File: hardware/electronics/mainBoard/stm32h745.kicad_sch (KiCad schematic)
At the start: 54 parts, among them SW1 PTS810, SW2 PTS810, U1 STM32H745ZIT6

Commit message: debugger stuff
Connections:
- net EEPROM_WC: now also U1.28 (PC0); no longer U1.127 (PG14)
- net H7_LEDBUILTIN: now also U1.40 (PA3); no longer U1.37 (PA0)
- net LTE.PWR_EN: now also U1.9 (PC13); no longer U1.5 (PE6)
- net LTE.RST: now also U1.5 (PE6); no longer U1.1 (PE2)
- net QSPI1.IO2: now also U1.1 (PE2); no longer U1.21 (PF7)
- net SDMMC2.CMD: now also U1.37 (PA0); no longer U1.121 (PD7)
- net USART6.TX: now also U1.127 (PG14); no longer U1.93 (PC6)
- net UART7.RX: now reaches U1.57 (PE7)
- net L0_NRST renamed L0_nRST
- new net UART7.TX: U1.21 (PF7)
- no-connect marks 31 -> 29
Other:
- note added: "Check CANBus RX/RX In/Out"
- moved on the sheet: D1, R1

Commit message: nets
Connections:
- net H7_NRST: no longer C1.1, D2.1, SW1.1, SW1.2, U1.27 (NRST)
- net 25MHz renamed H7_25MHz
- net 32768Hz renamed H7_32768Hz
- new net H7_nRST: C1.1, D2.1, SW1.1, SW1.2, U1.27 (NRST)
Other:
- note removed: "Check CANBus RX/RX In/Out"
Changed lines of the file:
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@@
 		)
 	)
-	(text "Check CANBus RX/RX In/Out"
-		(exclude_from_sim no)
-		(at 92.71 60.96 0)
-		(effects
-			(font
-				(size 1.27 1.27)
-			)
-		)
-	)
 	(text "AUX Card GPIO"
 		(exclude_from_sim no)
@@
 		)
 	)
-	(label "25MHz"
+	(label "H7_25MHz"
 		(at 171.45 45.72 180)
 		(effects
@@
 		)
 	)
-	(label "H7_NRST"
+	(label "H7_nRST"
 		(at 168.91 71.12 180)
 		(effects
@@
 		)
 	)
-	(label "32768Hz"
+	(label "H7_32768Hz"
 		(at 93.98 55.88 180)
 		(effects
@@
 		)
 	)
-	(hierarchical_label "25MHz"
+	(hierarchical_label "H7_25MHz"
 		(shape input)
 		(at 171.45 45.72 0)
@@
 		)
 	)
-	(hierarchical_label "32768Hz"
+	(hierarchical_label "H7_32768Hz"
 		(shape input)
 		(at 93.98 55.88 0)
@@
 		)
 	)
-	(hierarchical_label "H7_NRST"
+	(hierarchical_label "H7_nRST"
 		(shape input)
 		(at 171.45 71.12 0)
@@
 			(justify left bottom)
 		)
-		(property "Netclass" "MII"
+		(property "Netclass" "RMII"
 			(at 240.7285 13.97 0)
 			(effects

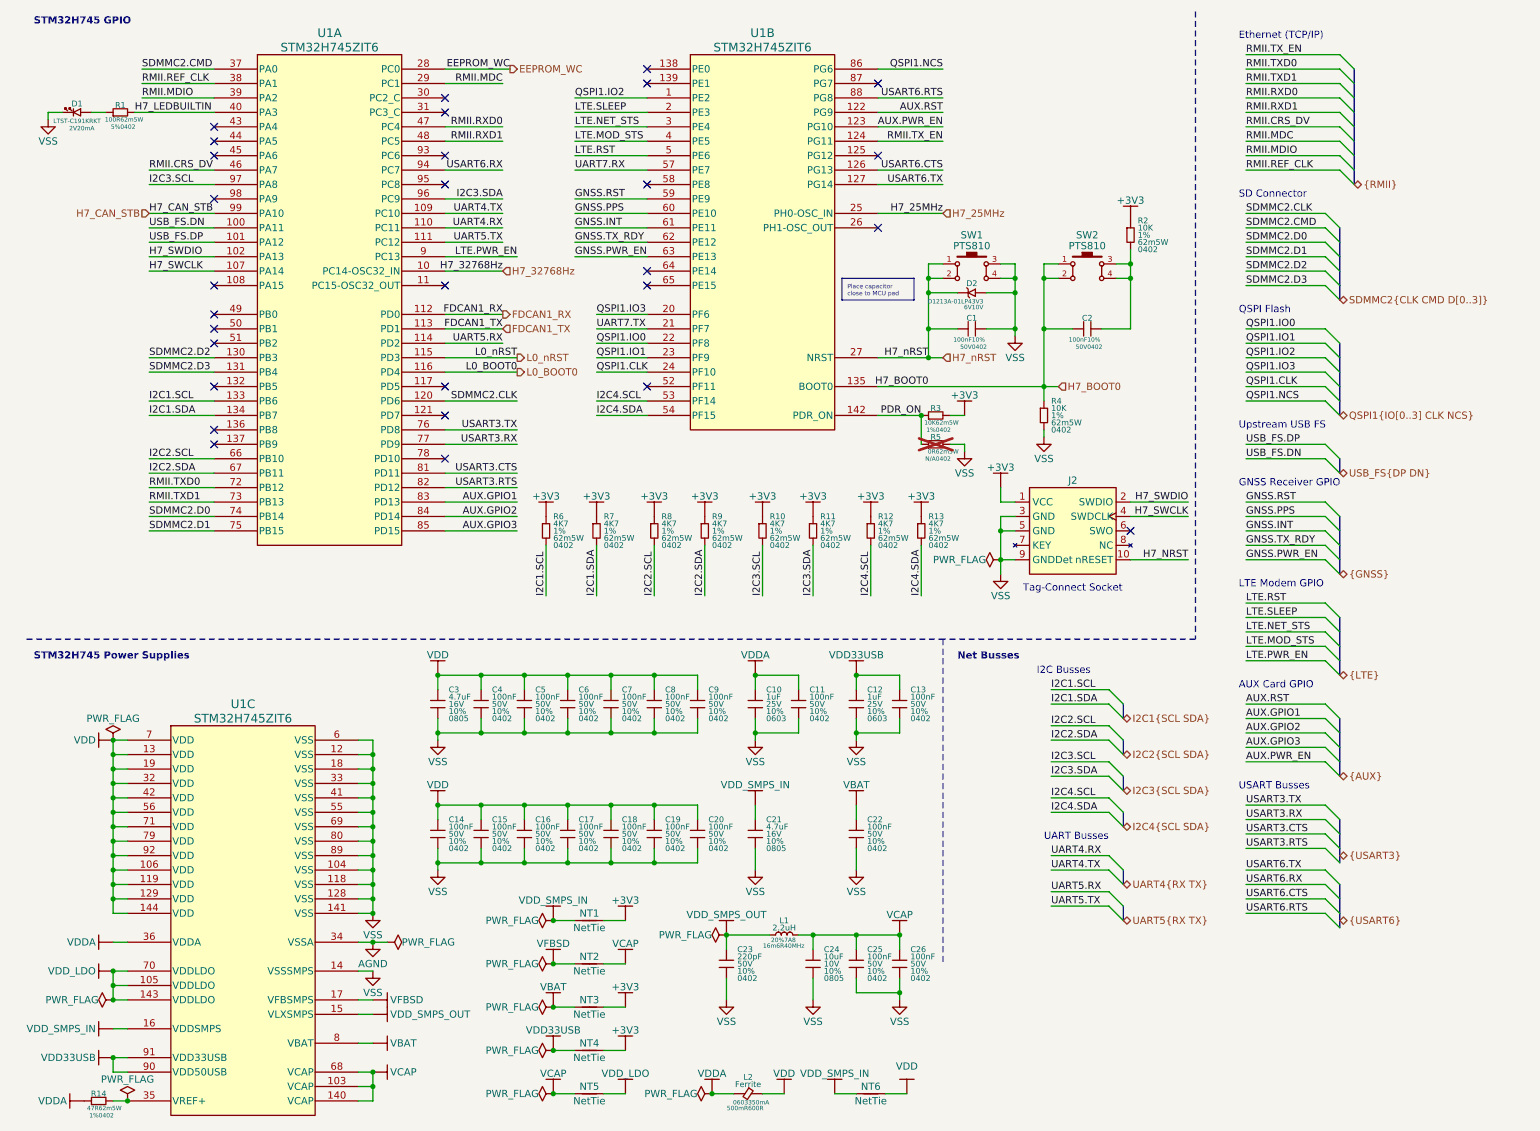
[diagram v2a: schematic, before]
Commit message: fixed net names
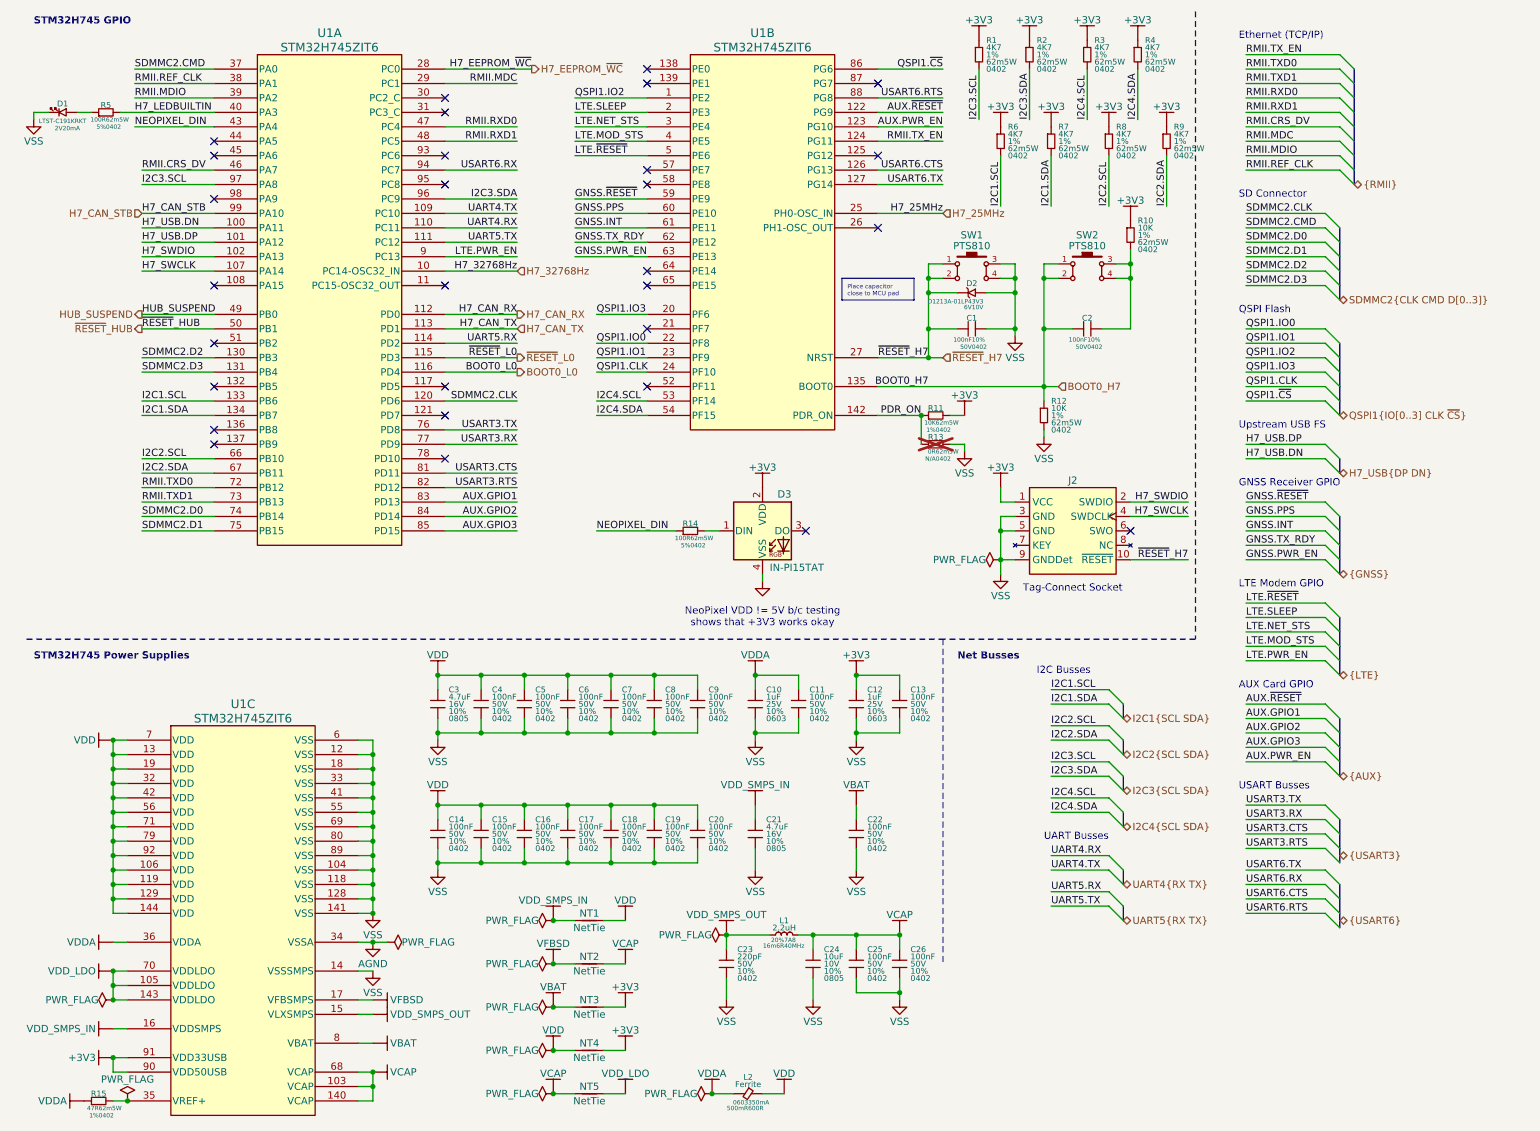
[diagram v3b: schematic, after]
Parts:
- removed NT6: NetTie, lib_misc:NetTie-2_SMD_Pad2.0mm, symbol lib_sch:NetTie
- added D3: IN-PI15TAT, lib_diodes:IN-PI15TAT, symbol lib_sch:Addressable LED
- added R14: 100R, lib_passives:CRCW0402, symbol lib_sch:R_horizontal
- renumbered R10 to R1, R2 to R10, R3 to R11, R4 to R12, R5 to R13, R14 to R15, R11 to R2, R12 to R3, R13 to R4, R1 to R5
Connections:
- net H7_nRST is gone; now on net ~{RESET}_H7: C1.1, D2.1, SW1.1, SW1.2, U1.27 (NRST)
- net +3V3: now also C12.1, C13.1, U1.90 (VDD50USB), U1.91 (VDD33USB), D3.2 (VDD); no longer NT1.2
- net VDD: now also NT1.2, NT4.1
- net VSS: now also D3.4 (VSS)
- net NEOPIXEL_DIN: now reaches U1.43 (PA4)
- net NEOPIXEL_DIN: now also R14.1
- net HUB_SUSPEND: now reaches U1.49 (PB0)
- net ~{RESET}_HUB: now reaches U1.50 (PB1)
- net AUX.RST renamed AUX.~{RESET}
- net EEPROM_WC renamed H7_EEPROM_~{WC}
- net FDCAN1_RX renamed H7_CAN_RX
- net FDCAN1_TX renamed H7_CAN_TX
- net GNSS.RST renamed GNSS.~{RESET}
- net H7_BOOT0 renamed BOOT0_H7
- net H7_NRST renamed ~{RESET}_H7
- net L0_BOOT0 renamed BOOT0_L0
- net L0_nRST renamed ~{RESET}_L0
- net LTE.RST renamed LTE.~{RESET}
- net QSPI1.NCS renamed QSPI1.~{CS}
- net UART7.RX: no longer names the net of U1.57 (PE7)
- net UART7.TX: no longer names the net of U1.21 (PF7)
- net USB_FS.DN renamed H7_USB.DN
- net USB_FS.DP renamed H7_USB.DP
- removed net VDD33USB: C12.1, C13.1, NT4.1, U1.90 (VDD50USB), U1.91 (VDD33USB)
- new net: D3.1 (DIN), R14.2
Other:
- note added: "NeoPixel VDD != 5V b/c testing shows that +3V3 works okay"
- moved on the sheet: D1, R1, R2, R3, R4, R5, R6, R7, R8, R9

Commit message: power supplies and organization
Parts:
- removed C1: 100nF, lib_passives:GCM0402, symbol lib_sch:C_horizontal
- removed C10, C12: 1uF, lib_passives:GRT0603, symbol lib_sch:C
- removed C11, C13, C22: 100nF, lib_passives:GCM0402, symbol lib_sch:C
- removed C21, C3: 4.7uF, lib_passives:GCM0805, symbol lib_sch:C
- removed NT1, NT2, NT3, NT4, NT5: NetTie, lib_misc:NetTie-2_SMD_Pad2.0mm, symbol lib_sch:NetTie
- added C148, C149, C152, C155, C159, C160: 100nF, lib_passives:GCM0402, symbol lib_sch:C
- added C150: 1uF, lib_passives:GRT0603, symbol lib_sch:C
- added C151, C154: 4.7uF, lib_passives:GCM0805, symbol lib_sch:C
- added C153, C158: 10uF, lib_passives:GCM0805, symbol lib_sch:C
- added C156, C157: 2.2uF, lib_passives:GCM0805, symbol lib_sch:C
- added C3: 100nF, lib_passives:GCM0402, symbol lib_sch:C_horizontal
- added JP9: Jumper_3_Bridged12, symbol lib_sch:Jumper_3_Bridged12
- U1: footprint lib_ICs:LQFP-144 -> LQFP-144
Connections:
- net AGND is gone; now on net VSS: U1.34 (VSSA)
- net VBAT is gone; now on net +3V3: U1.8 (VBAT)
- net VDD_SMPS_IN is gone; now on net +3V3: U1.16 (VDDSMPS)
- net +3V3: now also C14.1, C15.1, C16.1, C17.1, C18.1, C19.1, C20.1, C4.1, C5.1, C6.1, C7.1, C8.1, C9.1, L2.1, U1.106 (VDD), U1.119 (VDD), U1.129 (VDD), U1.13 (VDD), U1.144 (VDD), U1.19 (VDD), U1.32 (VDD), U1.42 (VDD), U1.56 (VDD), U1.7 (VDD), U1.71 (VDD), U1.79 (VDD), U1.92 (VDD), C148.1, C150.1, C151.1, C153.1, C154.1, C155.1, C160.1
- net I2C2.SCL: now also R9.2; no longer R8.2
- net I2C2.SDA: now also R8.2; no longer R9.2
- net VCAP: now also C156.1, C157.1, JP9.1 (A); no longer C24.1, L1.2
- net VDDA: now also L2.2, C158.1, C159.1; no longer L2.1
- net VDD_LDO: now also C149.1, C152.1, JP9.3 (B)
- net VSS: now also C148.2, C149.2, C150.2, C151.2, C152.2, C153.2, C154.2, C155.2, C156.2, C157.2, C158.2, C159.2, C160.2, C3.2
- net ~{RESET}_H7: now also C3.1
- removed net VDD: C14.1, C15.1, C16.1, C17.1, C18.1, C19.1, C20.1, C4.1, C5.1, C6.1, C7.1, C8.1, C9.1, L2.2, U1.106 (VDD), U1.119 (VDD), U1.129 (VDD), U1.13 (VDD), U1.144 (VDD), U1.19 (VDD), U1.32 (VDD), U1.42 (VDD), U1.56 (VDD), U1.7 (VDD), U1.71 (VDD), U1.79 (VDD), U1.92 (VDD)
- net VDD_SMPS_OUT: no longer names the net of C23.1, U1.15 (VLXSMPS)
- net VDD_SMPS_OUT: now also L1.2; no longer L1.1
- net VFBSD renamed SMPS_FB
- net SMPS_FB: now also C24.1, L1.1, JP9.2 (C)
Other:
- note added: "M.2 GPIO"
- note added: "VBAT"
- note added: "VDD"
- note added: "VDDA"
- note added: "VDDLDO"
- note added: "VDDSMPS"
- note added: "VDDUSB"
- note removed: "AUX Card GPIO"
- note removed: "GNSS Receiver GPIO"
- note removed: "LTE Modem GPIO"
- moved on the sheet: C14, C15, C16, C17, C18, C19, C2, C20, C23, C24, C25, C26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

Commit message: organized page. Added SPI and other nets
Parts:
- added Q1: BSS138-7-F, lib_ICs:SOT23, symbol lib_sch:NMOS_GSD
- JP1: renamed from JP9; footprint (none) -> lib_misc:SolderJumper-3_P1.3mm_Bridged12_RoundedPad1.0x1.5mm
- L1: renamed from L2; now not fitted
- R14: renamed from R5; value 100R -> 412R; DKPN 541-100JCT-ND -> 541-412LCT-ND; MPN CRCW0402100RJNED -> CRCW0402412RFKED
- U1: footprint LQFP-144 -> lib_ICs:LQFP-144
- renumbered C3 to C1, C14 to C10, C15 to C11, C16 to C12, C17 to C13, C18 to C14, C19 to C15, C20 to C16, C153 to C17, C158 to C18, C159 to C19, C154 to C20, C155 to C21, C150 to C22, C148 to C23, C149 to C24, C152 to C25, C160 to C26, C24 to C27, C23 to C28, C156 to C29, C151 to C3, C157 to C30, C26 to C31, C25 to C32, D2 to D1, D3 to D2, D1 to D3, L1 to L2, R11 to R10, R12 to R11, R13 to R12, R14 to R13, R10 to R3, R8 to R4, R9 to R5, R7 to R6, R6 to R7, R4 to R8, R3 to R9
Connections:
- net H7_LEDBUILTIN: now also R14.1, U1.136 (PB8); no longer R14.2, U1.40 (PA3)
- net NEOPIXEL_DIN: now also U1.137 (PB9); no longer U1.43 (PA4)
- net QSPI1.IO2: now also U1.21 (PF7); no longer U1.1 (PE2)
- net VSS: now also Q1.2
- net ~{RESET}_L0: now also Q1.1, Q1.3
- net at D3.1: now also R14.2; no longer R14.1
- net SPI1.~{SS}_L0: now reaches U1.117 (PD5)
- net SPI1.MOSI: now reaches U1.121 (PD7)
- net SPI1.GRANT: now reaches U1.30 (PC2_C)
- net SPI1.REQ: now reaches U1.31 (PC3_C)
- net SPI1.SCK: now reaches U1.44 (PA5)
- net SPI1.MISO: now reaches U1.45 (PA6)
- net HUB_H7_INT: now reaches U1.51 (PB2)
- net H7_25MHz renamed 25MHz
- net H7_32768Hz renamed 32768Hz
- new net SPI1.~{SS}_H7: U1.43 (PA4)
- new net ~{RESET}_ETH: U1.40 (PA3)
- no-connect marks 29 -> 20
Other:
- note removed: "NeoPixel VDD != 5V b/c testing shows that +3V3 works okay"
- title: STM32H745 I/Os -> Awohali - STM32H745
- moved on the sheet: C10, C11, C12, C13, C14, C15, C16, C17, C18, C19, C20, C21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
